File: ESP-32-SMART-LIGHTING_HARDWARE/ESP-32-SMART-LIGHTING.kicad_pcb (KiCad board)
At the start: 2 copper layers, 12 parts, among them J1 PSU, J2 Screw_Terminal_01x02, J3 Screw_Terminal_01x02, Q1 IRL540N, Q2 IRL540N, U1 ESP32-S3-DEVKITC-1-N8R2, U2 INMP41, U3 INMP41

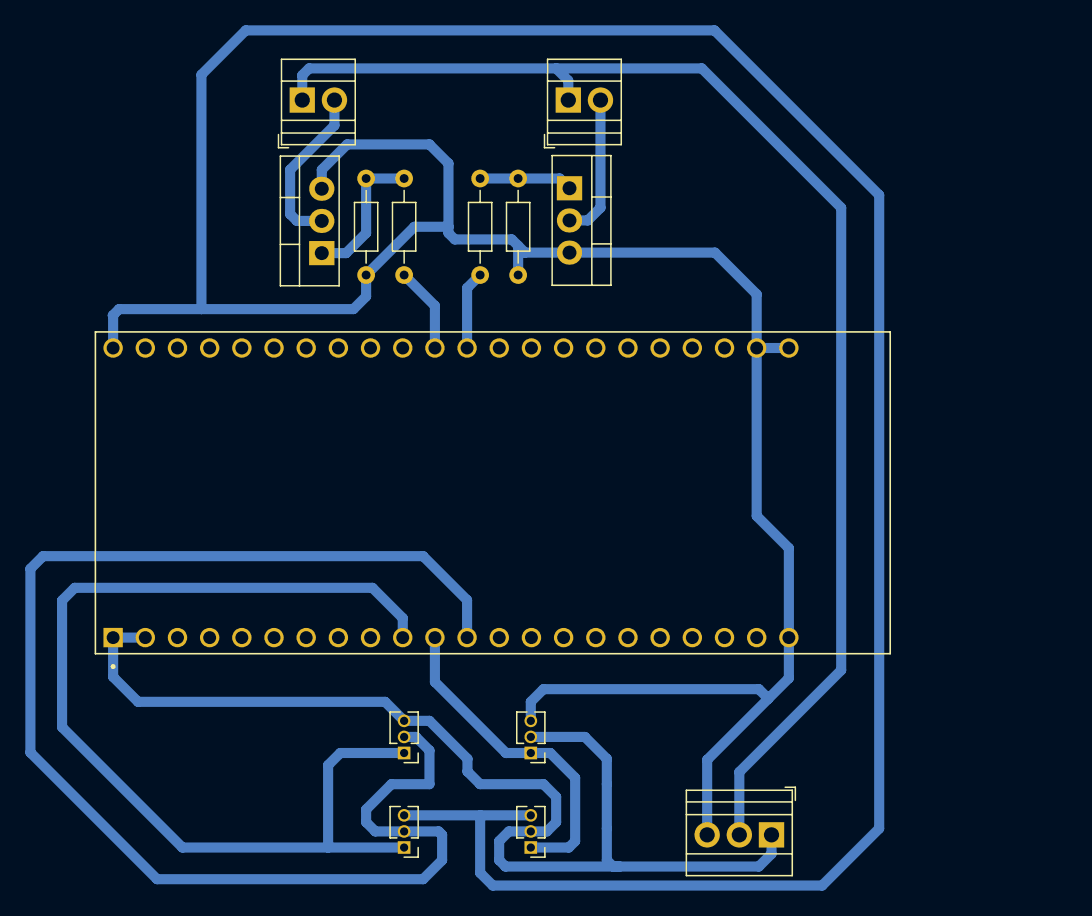
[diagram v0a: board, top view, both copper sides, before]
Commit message: Fixed PCB size, fixed module size
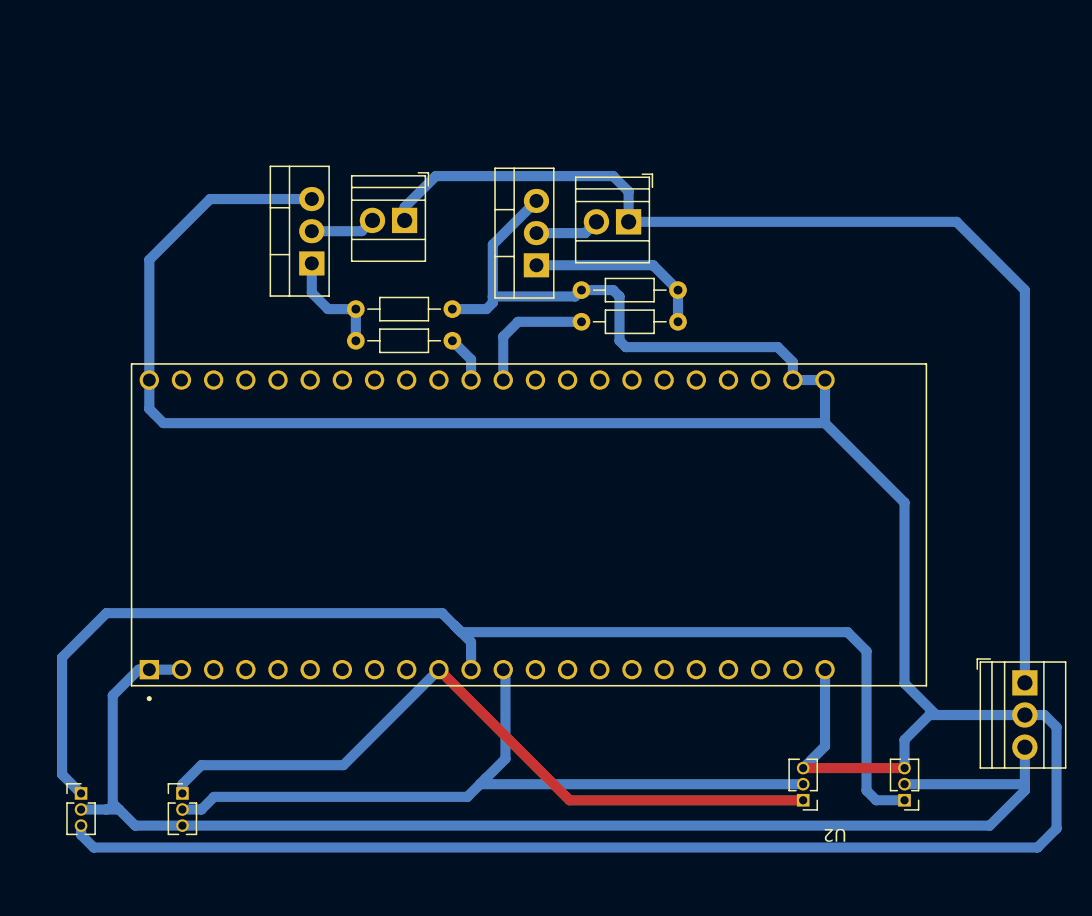
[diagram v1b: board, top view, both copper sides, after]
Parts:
- moved U3 31.4 mm to (93.0, 117.5), turned to 0 degrees
- moved U2 29.7 mm to (153.0, 128.5)
- moved J1 23.3 mm to (165.0, 114.0), turned to -90 degrees
- moved J3 12.5 mm to (116.0, 77.5), turned to 180 degrees
- moved J2 10.7 mm to (133.7, 77.6), turned to 180 degrees
- moved R1 8.81 mm to (130.0, 85.5), turned to 0 degrees
- moved R4 7.32 mm to (119.8, 84.5), turned to 180 degrees
- moved Q1 6.62 mm to (126.4, 81.0), turned to 90 degrees
- moved R3 6.44 mm to (119.8, 87.0), turned to 180 degrees
- moved R2 5.14 mm to (130.0, 83.0), turned to 0 degrees
- moved U1 3.81 mm to (125.9, 101.5)
- moved Q2 1.13 mm to (108.7, 80.9)
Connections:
- J1 pad 1: +3.3V -> +12V
- J1 pad 2: +12V -> GND
- J1 pad 3: GND -> +3.3V
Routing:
- net /I2S_SD: track 26.4 -> 95.9 mm
- net GND: track 327.1 -> 274.3 mm
- net /I2S_WS: track 111.4 -> 60.0 mm
- net /I2S_SCK: track 83.7 -> 57.7 mm
- net +12V: track 105.0 -> 87.1 mm
- net +3.3V: track 93.3 -> 104.6 mm
- net Net-(J3-Pin_2): track 13.2 -> 5.14 mm
- net /MCU_PWM_1_GATE: track 7.37 -> 14.5 mm
- net Net-(J2-Pin_2): track 11.4 -> 5.10 mm
- net /MCU_PWM_1: track 6.19 -> 10.1 mm
- net /MCU_PWM_2: track 6.77 -> 3.71 mm
- net /MCU_PWM_2_GATE: track 11.5 -> 8.83 mm
